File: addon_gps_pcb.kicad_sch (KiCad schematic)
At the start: 14 parts, among them J10 WS2812B, J14 5V GPIO Breakout, J9 2x8, U7 SAM-M10Q, U8 TXB0104QPWRQ1

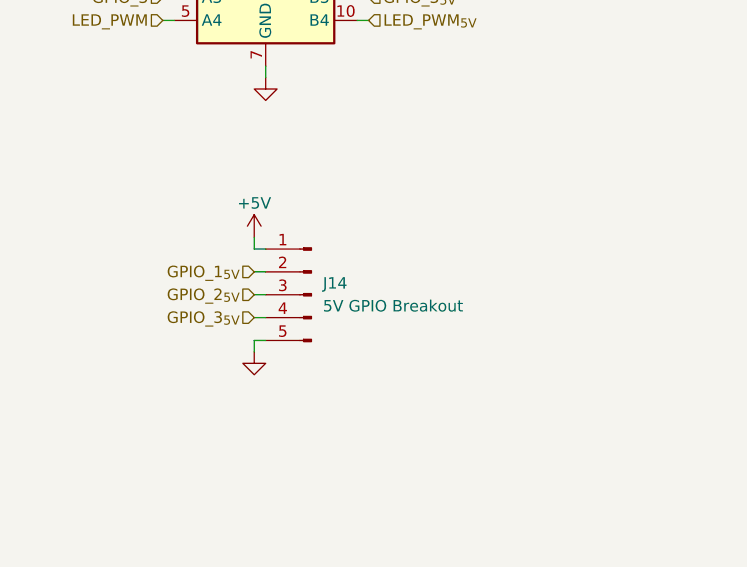
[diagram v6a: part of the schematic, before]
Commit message: Clean up schematics and add footprints
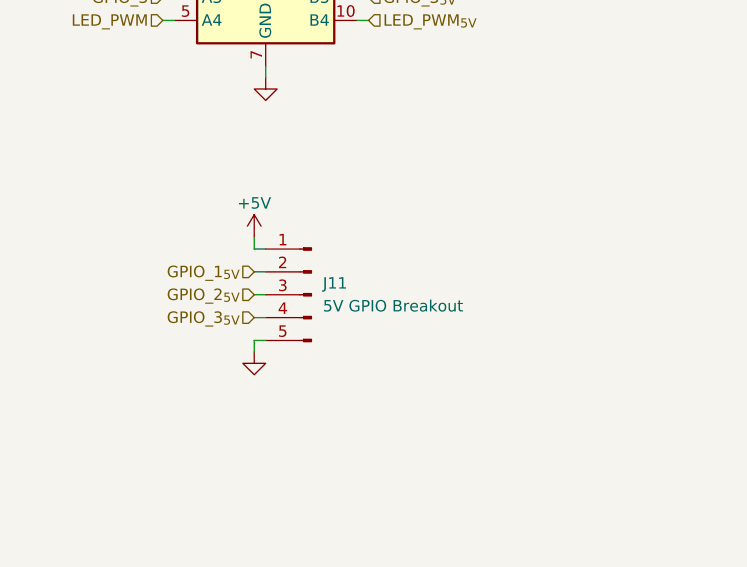
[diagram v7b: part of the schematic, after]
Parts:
- J11: renamed from J14; footprint (none) -> Connector_PinHeader_2.54mm:PinHeader_1x05_P2.54mm_Vertical
- J9: footprint (none) -> Connector_PinHeader_2.54mm:PinHeader_2x08_P2.54mm_Vertical
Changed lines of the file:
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@@
 		(on_board yes)
 		(dnp no)
-		(property "Reference" "#PWR0144"
+		(property "Reference" "#PWR0107"
 			(at 44.45 132.08 0)
 			(effects
@@
 			(project "nerve_pcb"
 				(path "/c0277862-b3f2-4e0e-986f-34702f0543f0/5e5db2cb-8fc9-48f2-985b-a0cd6e1a3554"
-					(reference "#PWR0144")
+					(reference "#PWR0107")
 					(unit 1)
 				)
@@
 		(dnp no)
 		(fields_autoplaced yes)
-		(property "Reference" "J14"
+		(property "Reference" "J11"
 			(at 52.07 133.3499 0)
 			(effects
@@
 			)
 		)
-		(property "Footprint" ""
+		(property "Footprint" "Connector_PinHeader_2.54mm:PinHeader_1x05_P2.54mm_Vertical"
 			(at 50.8 134.62 0)
 			(effects
@@
 			(project ""
 				(path "/c0277862-b3f2-4e0e-986f-34702f0543f0/5e5db2cb-8fc9-48f2-985b-a0cd6e1a3554"
-					(reference "J14")
+					(reference "J11")
 					(unit 1)
 				)
@@
 		(dnp no)
 		(fields_autoplaced yes)
-		(property "Reference" "#PWR0108"
+		(property "Reference" "#PWR0110"
 			(at 252.73 168.91 0)
 			(effects
@@
 			(project "nerve_pcb"
 				(path "/c0277862-b3f2-4e0e-986f-34702f0543f0/5e5db2cb-8fc9-48f2-985b-a0cd6e1a3554"
-					(reference "#PWR0108")
+					(reference "#PWR0110")
 					(unit 1)
 				)
@@
 		(dnp no)
 		(fields_autoplaced yes)
-		(property "Reference" "#PWR0109"
+		(property "Reference" "#PWR0111"
 			(at 265.43 168.91 0)
 			(effects
@@
 			(project "nerve_pcb"
 				(path "/c0277862-b3f2-4e0e-986f-34702f0543f0/5e5db2cb-8fc9-48f2-985b-a0cd6e1a3554"
-					(reference "#PWR0109")
+					(reference "#PWR0111")
 					(unit 1)
 				)
@@
 		(dnp no)
 		(fields_autoplaced yes)
-		(property "Reference" "#PWR0145"
+		(property "Reference" "#PWR0108"
 			(at 44.45 147.32 0)
 			(effects
@@
 			(project "nerve_pcb"
 				(path "/c0277862-b3f2-4e0e-986f-34702f0543f0/5e5db2cb-8fc9-48f2-985b-a0cd6e1a3554"
-					(reference "#PWR0145")
+					(reference "#PWR0108")
 					(unit 1)
 				)
@@
 			)
 		)
-		(property "Footprint" ""
+		(property "Footprint" "Connector_PinHeader_2.54mm:PinHeader_2x08_P2.54mm_Vertical"
 			(at 246.38 33.02 0)
 			(effects
@@
 		(dnp no)
 		(fields_autoplaced yes)
-		(property "Reference" "#PWR0107"
+		(property "Reference" "#PWR0109"
 			(at 240.03 168.91 0)
 			(effects
@@
 			(project "nerve_pcb"
 				(path "/c0277862-b3f2-4e0e-986f-34702f0543f0/5e5db2cb-8fc9-48f2-985b-a0cd6e1a3554"
-					(reference "#PWR0107")
+					(reference "#PWR0109")
 					(unit 1)
 				)
@@
 		(dnp no)
 		(fields_autoplaced yes)
-		(property "Reference" "#PWR0110"
+		(property "Reference" "#PWR0112"
 			(at 278.13 168.91 0)
 			(effects
@@
 			(project "nerve_pcb"
 				(path "/c0277862-b3f2-4e0e-986f-34702f0543f0/5e5db2cb-8fc9-48f2-985b-a0cd6e1a3554"
-					(reference "#PWR0110")
-					(unit 1)
-				)
+					(reference "#PWR0112")
+					(unit 1)
+				)

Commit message: Swap to 1.27mm board-to-board and WIP PCB
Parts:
- J9: footprint Connector_PinHeader_2.54mm:PinHeader_2x08_P2.54mm_Vertical -> Connector_PinHeader_1.27mm:PinHeader_2x08_P1.27mm_Vertical_SMD
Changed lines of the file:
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@@
 			)
 		)
-		(property "Footprint" "Connector_PinHeader_2.54mm:PinHeader_2x08_P2.54mm_Vertical"
+		(property "Footprint" "Connector_PinHeader_1.27mm:PinHeader_2x08_P1.27mm_Vertical_SMD"
 			(at 246.38 33.02 0)
 			(effects
